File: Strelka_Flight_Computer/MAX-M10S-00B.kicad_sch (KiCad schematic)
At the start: 17 parts, among them IC2 MAX-M10S-00B

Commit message: Started design for V2
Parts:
- removed AE2: Antenna_Shield, Connector_Coaxial:U.FL_Hirose_U.FL-R-SMT-1_Vertical, symbol Device:Antenna_Shield
- removed JP2: UART_Switch, Footprints:UART_Switch, symbol UART_Switch:UART_Switch
- added AE1: Antenna_Shield, Footprints:STA-10201, symbol Device:Antenna_Shield
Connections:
- net GND: now also AE1.2 (Shield)
- net RF_IN: now also AE1.1 (A)
- net UBLOX_UART_RX: now also IC2.3 (RXD)
- net UBLOX_UART_TX: now also IC2.2 (TXD)
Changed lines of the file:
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@@
-    (stroke (width 0) (type default))
-  )
-  (wire (pts (xy 190.5 99.06) (xy 190.5 98.425))
-    (stroke (width 0) (type default))
-  )
-  (wire (pts (xy 190.5 102.235) (xy 194.31 102.235))
     (stroke (width 0) (type default))
   )
@@
     (stroke (width 0) (type default))
   )
-  (wire (pts (xy 190.5 98.425) (xy 194.31 98.425))
-    (stroke (width 0) (type default))
-  )
   (wire (pts (xy 53.975 102.235) (xy 53.975 104.14))
     (stroke (width 0) (type default))
@@
     (stroke (width 0) (type default))
   )
-  (wire (pts (xy 174.625 101.6) (xy 190.5 101.6))
+  (wire (pts (xy 174.625 101.6) (xy 192.405 101.6))
     (stroke (width 0) (type default))
   )
@@
     (stroke (width 0) (type default))
   )
-  (wire (pts (xy 209.55 102.235) (xy 211.455 102.235))
-    (stroke (width 0) (type default))
-  )
   (wire (pts (xy 67.945 162.56) (xy 67.945 163.195))
     (stroke (width 0) (type default))
@@
     (stroke (width 0) (type default))
   )
-  (wire (pts (xy 209.55 98.425) (xy 211.455 98.425))
-    (stroke (width 0) (type default))
-  )
   (wire (pts (xy 57.785 160.02) (xy 57.785 163.195))
     (stroke (width 0) (type default))
@@
     (stroke (width 0) (type default))
   )
-  (wire (pts (xy 174.625 99.06) (xy 190.5 99.06))
+  (wire (pts (xy 174.625 99.06) (xy 192.405 99.06))
     (stroke (width 0) (type default))
   )
@@
   )
   (wire (pts (xy 48.895 154.305) (xy 48.895 153.67))
-    (stroke (width 0) (type default))
-  )
-  (wire (pts (xy 190.5 101.6) (xy 190.5 102.235))
     (stroke (width 0) (type default))
   )
@@
     (effects (font (size 1.27 1.27)) (justify left))
   )
-  (hierarchical_label "UBLOX_UART_RX" (shape input) (at 211.455 98.425 0) (fields_autoplaced)
+  (hierarchical_label "UBLOX_UART_RX" (shape input) (at 192.405 99.06 0) (fields_autoplaced)
     (effects (font (size 1.27 1.27)) (justify left))
   )
@@
     (effects (font (size 1.27 1.27)) (justify left))
   )
-  (hierarchical_label "UBLOX_UART_TX" (shape input) (at 211.455 102.235 0) (fields_autoplaced)
+  (hierarchical_label "UBLOX_UART_TX" (shape input) (at 192.405 101.6 0) (fields_autoplaced)
     (effects (font (size 1.27 1.27)) (justify left))
   )
@@
     )
   )
-  (symbol (lib_id "UART_Switch:UART_Switch") (at 201.93 100.965 0) (unit 1)
-    (in_bom yes) (on_board yes) (dnp no)
-    (property "Reference" "JP2" (at 201.93 92.71 0)
-      (effects (font (size 1.27 1.27)))
-    )
-    (property "Value" "UART_Switch" (at 201.93 95.25 0)
-      (effects (font (size 1.27 1.27)))
-    )
-    (property "Footprint" "Footprints:UART_Switch" (at 201.93 100.965 0)
-      (effects (font (size 1.27 1.27)) hide)
-    )
-    (property "Datasheet" "" (at 201.93 100.965 0)
-      (effects (font (size 1.27 1.27)) hide)
-    )
-    (pin "1")
-    (pin "2")
-    (pin "3")
-    (pin "4")
-    (instances
-      (project "Strelka_Flight_Computer"
-        (path "/e63e39d7-6ac0-4ffd-8aa3-1841a4541b55/78f71895-bddb-4f64-a608-99074f2d1c44/139c9d95-fce8-4012-aeed-de926a08d12b"
-          (reference "JP2") (unit 1)
+  (symbol (lib_id "Device:Antenna_Shield") (at 35.56 71.12 0) (unit 1)
+    (in_bom yes) (on_board yes) (dnp no) (fields_autoplaced)
+    (property "Reference" "AE1" (at 39.1161 70.3385 0)
+      (effects (font (size 1.27 1.27)) (justify left))
+    )
+    (property "Value" "Antenna_Shield" (at 39.1161 73.1136 0)
+      (effects (font (size 1.27 1.27)) (justify left))
+    )
+    (property "Footprint" "Footprints:STA-10201" (at 35.56 68.58 0)
+      (effects (font (size 1.27 1.27)) hide)
+    )
+    (property "Datasheet" "https://datasheet.lcsc.com/lcsc/2111030930_STA-STA-10201_C2913580.pdf" (at 35.56 68.58 0)
+      (effects (font (size 1.27 1.27)) hide)
+    )
+    (property "LCSC#" "C2913580" (at 35.56 71.12 0)
+      (effects (font (size 1.27 1.27)) hide)
+    )
+    (pin "1")
+    (pin "2")
+    (instances
+      (project "Strelka_Flight_Computer"
+        (path "/e63e39d7-6ac0-4ffd-8aa3-1841a4541b55/72745e37-6398-4523-a0b8-fcae44c9df22"
+          (reference "AE1") (unit 1)
+        )
+        (path "/e63e39d7-6ac0-4ffd-8aa3-1841a4541b55/78f71895-bddb-4f64-a608-99074f2d1c44/139c9d95-fce8-4012-aeed-de926a08d12b"
+          (reference "AE2") (unit 1)
         )
       )
@@
         )
       )
-    )
-  )
-  (symbol (lib_id "Device:Antenna_Shield") (at 35.56 71.12 0) (unit 1)
-    (in_bom yes) (on_board yes) (dnp no) (fields_autoplaced)
-    (property "Reference" "AE2" (at 38.735 69.6503 0)
-      (effects (font (size 1.27 1.27)) (justify left))
-    )
-    (property "Value" "Antenna_Shield" (at 38.735 72.1872 0)
-      (effects (font (size 1.27 1.27)) (justify left))
-    )
-    (property "Footprint" "Connector_Coaxial:U.FL_Hirose_U.FL-R-SMT-1_Vertical" (at 35.56 68.58 0)
-      (effects (font (size 1.27 1.27)) hide)
-    )
-    (property "Datasheet" "~" (at 35.56 68.58 0)
-      (effects (font (size 1.27 1.27)) hide)
-    )
-    (property "LCSC#" "C88373" (at 35.56 71.12 0)
-      (effects (font (size 1.27 1.27)) hide)
-    )
-    (pin "1")
-    (pin "2")
-    (instances
-      (project "Strelka_Flight_Computer"
-        (path "/e63e39d7-6ac0-4ffd-8aa3-1841a4541b55/78f71895-bddb-4f64-a608-99074f2d1c44/139c9d95-fce8-4012-aeed-de926a08d12b"
-          (reference "AE2") (unit 1)
-        )
-      )

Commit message: Changed design rules
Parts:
- C36, C38, C39, C40: footprint Capacitor_SMD:C_0603_1608Metric -> Capacitor_SMD:C_0402_1005Metric
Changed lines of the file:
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@@
       (effects (font (size 1.27 1.27)) (justify left))
     )
-    (property "Footprint" "Capacitor_SMD:C_0603_1608Metric" (at 218.44 88.9 0)
+    (property "Footprint" "Capacitor_SMD:C_0402_1005Metric" (at 218.44 88.9 0)
       (effects (font (size 1.27 1.27)) hide)
     )
@@
       (effects (font (size 1.27 1.27)) (justify left))
     )
-    (property "Footprint" "Capacitor_SMD:C_0603_1608Metric" (at 207.01 88.9 0)
+    (property "Footprint" "Capacitor_SMD:C_0402_1005Metric" (at 207.01 88.9 0)
       (effects (font (size 1.27 1.27)) hide)
     )
@@
       (effects (font (size 1.27 1.27)) (justify left))
     )
-    (property "Footprint" "Capacitor_SMD:C_0603_1608Metric" (at 57.785 157.48 0)
+    (property "Footprint" "Capacitor_SMD:C_0402_1005Metric" (at 57.785 157.48 0)
       (effects (font (size 1.27 1.27)) hide)
     )
@@
       (effects (font (size 1.27 1.27)) (justify left))
     )
-    (property "Footprint" "Capacitor_SMD:C_0603_1608Metric" (at 48.895 156.845 0)
-      (effects (font (size 1.27 1.27)) hide)
-    )
+    (property "Footprint" "Capacitor_SMD:C_0402_1005Metric" (at 48.895 156.845 0)
+      (effects (font (size 1.27 1.27)) hide)
+    )

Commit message: Routing starting
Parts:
- removed R58: 0R, Resistor_SMD:R_0603_1608Metric, symbol Device:R_Small
- R56, R57: footprint Resistor_SMD:R_0603_1608Metric -> Resistor_SMD:R_0402_1005Metric
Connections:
- net PPS is gone; now on net TIMEPULSE: IC2.4 (TIMEPULSE), R57.1
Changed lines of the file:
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@@
     (stroke (width 0) (type default))
   )
-  (wire (pts (xy 214.63 111.76) (xy 217.17 111.76))
+  (wire (pts (xy 214.63 111.76) (xy 222.25 111.76))
     (stroke (width 0) (type default))
   )
@@
         (path "/e63e39d7-6ac0-4ffd-8aa3-1841a4541b55/78f71895-bddb-4f64-a608-99074f2d1c44/139c9d95-fce8-4012-aeed-de926a08d12b"
           (reference "BT2") (unit 1)
-        )
-      )
-    )
-  )
-  (symbol (lib_id "Device:R_Small") (at 219.71 111.76 90) (unit 1)
-    (in_bom yes) (on_board yes) (dnp no)
-    (property "Reference" "R58" (at 218.5416 110.2614 0)
-      (effects (font (size 1.27 1.27)) (justify left))
-    )
-    (property "Value" "0R" (at 220.853 110.2614 0)
-      (effects (font (size 1.27 1.27)) (justify left))
-    )
-    (property "Footprint" "Resistor_SMD:R_0603_1608Metric" (at 219.71 111.76 0)
-      (effects (font (size 1.27 1.27)) hide)
-    )
-    (property "Datasheet" "~" (at 219.71 111.76 0)
-      (effects (font (size 1.27 1.27)) hide)
-    )
-    (pin "1")
-    (pin "2")
-    (instances
-      (project "Strelka_Flight_Computer"
-        (path "/e63e39d7-6ac0-4ffd-8aa3-1841a4541b55/78f71895-bddb-4f64-a608-99074f2d1c44/139c9d95-fce8-4012-aeed-de926a08d12b"
-          (reference "R58") (unit 1)
         )
       )
@@
       (effects (font (size 1.27 1.27)) (justify left))
     )
-    (property "Footprint" "Resistor_SMD:R_0603_1608Metric" (at 67.945 149.86 0)
+    (property "Footprint" "Resistor_SMD:R_0402_1005Metric" (at 67.945 149.86 0)
       (effects (font (size 1.27 1.27)) hide)
     )
@@
       (effects (font (size 1.27 1.27)) (justify left))
     )
-    (property "Footprint" "Resistor_SMD:R_0603_1608Metric" (at 214.63 114.935 0)
-      (effects (font (size 1.27 1.27)) hide)
-    )
+    (property "Footprint" "Resistor_SMD:R_0402_1005Metric" (at 214.63 114.935 0)
+      (effects (font (size 1.27 1.27)) hide)
+    )

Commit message: Continued routing
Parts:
- C37: now not fitted
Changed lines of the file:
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@@
   )
   (symbol (lib_id "Device:C_Small") (at 53.975 107.315 0) (unit 1)
-    (in_bom yes) (on_board yes) (dnp no)
+    (in_bom yes) (on_board yes) (dnp yes)
     (property "Reference" "C37" (at 56.515 104.775 0)
       (effects (font (size 1.27 1.27)) (justify left))

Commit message: Routing complete
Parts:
- removed C36: 100n, Capacitor_SMD:C_0402_1005Metric, symbol Device:C_Small
- D12: value LED_BLUE -> LED_GREEN; LCSC (none) -> C72043
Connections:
- net +3V3 renamed +3.3V
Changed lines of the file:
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@@
 (kicad_sch (version 20230121) (generator eeschema)
   (paper "A4")
+  (junction (at 212.725 83.82) (diameter 0) (color 0 0 0 0)
+  )
   (junction (at 177.165 86.36) (diameter 0) (color 0 0 0 0)
   )
@@
   (junction (at 213.36 91.44) (diameter 0) (color 0 0 0 0)
   )
-  (junction (at 213.36 83.82) (diameter 0) (color 0 0 0 0)
-  )
   (junction (at 57.785 153.67) (diameter 0) (color 0 0 0 0)
   )
   (junction (at 62.865 163.195) (diameter 0) (color 0 0 0 0)
-  )
-  (junction (at 57.785 163.195) (diameter 0) (color 0 0 0 0)
   )
   (junction (at 53.975 104.14) (diameter 0) (color 0 0 0 0)
@@
     (stroke (width 0) (type default))
   )
-  (wire (pts (xy 48.895 159.385) (xy 48.895 163.195))
-    (stroke (width 0) (type default))
-  )
   (wire (pts (xy 53.975 102.235) (xy 53.975 104.14))
     (stroke (width 0) (type default))
   )
-  (wire (pts (xy 48.895 163.195) (xy 57.785 163.195))
-    (stroke (width 0) (type default))
-  )
   (wire (pts (xy 53.975 104.14) (xy 60.96 104.14))
     (stroke (width 0) (type default))
@@
     (stroke (width 0) (type default))
   )
+  (wire (pts (xy 212.725 83.82) (xy 218.44 83.82))
+    (stroke (width 0) (type default))
+  )
   (wire (pts (xy 53.975 90.17) (xy 53.975 84.455))
     (stroke (width 0) (type default))
@@
     (stroke (width 0) (type default))
   )
-  (wire (pts (xy 48.895 153.67) (xy 57.785 153.67))
-    (stroke (width 0) (type default))
-  )
   (wire (pts (xy 57.785 160.02) (xy 57.785 163.195))
     (stroke (width 0) (type default))
@@
     (stroke (width 0) (type default))
   )
-  (wire (pts (xy 213.36 83.82) (xy 218.44 83.82))
+  (wire (pts (xy 207.01 83.82) (xy 212.725 83.82))
     (stroke (width 0) (type default))
   )
@@
     (stroke (width 0) (type default))
   )
-  (wire (pts (xy 48.895 154.305) (xy 48.895 153.67))
-    (stroke (width 0) (type default))
-  )
   (wire (pts (xy 57.785 153.67) (xy 67.945 153.67))
     (stroke (width 0) (type default))
@@
   )
   (wire (pts (xy 57.785 153.67) (xy 57.785 154.94))
-    (stroke (width 0) (type default))
-  )
-  (wire (pts (xy 207.01 83.82) (xy 213.36 83.82))
     (stroke (width 0) (type default))
   )
@@
         (path "/e63e39d7-6ac0-4ffd-8aa3-1841a4541b55/78f71895-bddb-4f64-a608-99074f2d1c44/139c9d95-fce8-4012-aeed-de926a08d12b"
           (reference "BT2") (unit 1)
+        )
+      )
+    )
+  )
+  (symbol (lib_name "+3.3V_1") (lib_id "power:+3.3V") (at 200.025 86.36 0) (unit 1)
+    (in_bom yes) (on_board yes) (dnp no) (fields_autoplaced)
+    (property "Reference" "#PWR015" (at 200.025 90.17 0)
+      (effects (font (size 1.27 1.27)) hide)
+    )
+    (property "Value" "+3.3V" (at 200.025 82.931 0)
+      (effects (font (size 1.27 1.27)))
+    )
+    (property "Footprint" "" (at 200.025 86.36 0)
+      (effects (font (size 1.27 1.27)) hide)
+    )
+    (property "Datasheet" "" (at 200.025 86.36 0)
+      (effects (font (size 1.27 1.27)) hide)
+    )
+    (pin "1")
+    (instances
+      (project "Strelka_Flight_Computer"
+        (path "/e63e39d7-6ac0-4ffd-8aa3-1841a4541b55/0daddb18-1491-4767-9ffd-66c8a8ce3cbd"
+          (reference "#PWR015") (unit 1)
+        )
+        (path "/e63e39d7-6ac0-4ffd-8aa3-1841a4541b55/78f71895-bddb-4f64-a608-99074f2d1c44/139c9d95-fce8-4012-aeed-de926a08d12b"
+          (reference "#PWR016") (unit 1)
         )
       )
@@
     )
   )
-  (symbol (lib_id "power:+3.3V") (at 200.025 86.36 0) (unit 1)
-    (in_bom yes) (on_board yes) (dnp no) (fields_autoplaced)
-    (property "Reference" "#PWR0210" (at 200.025 90.17 0)
-      (effects (font (size 1.27 1.27)) hide)
-    )
-    (property "Value" "+3.3V" (at 200.025 82.7842 0)
-      (effects (font (size 1.27 1.27)))
-    )
-    (property "Footprint" "" (at 200.025 86.36 0)
-      (effects (font (size 1.27 1.27)) hide)
-    )
-    (property "Datasheet" "" (at 200.025 86.36 0)
-      (effects (font (size 1.27 1.27)) hide)
-    )
-    (pin "1")
-    (instances
-      (project "Strelka_Flight_Computer"
-        (path "/e63e39d7-6ac0-4ffd-8aa3-1841a4541b55/78f71895-bddb-4f64-a608-99074f2d1c44/139c9d95-fce8-4012-aeed-de926a08d12b"
-          (reference "#PWR0210") (unit 1)
-        )
-      )
-    )
-  )
   (symbol (lib_id "Device:C_Small") (at 57.785 157.48 0) (unit 1)
     (in_bom yes) (on_board yes) (dnp no)
@@
     )
   )
-  (symbol (lib_id "power:+3.3V") (at 213.36 83.82 0) (unit 1)
-    (in_bom yes) (on_board yes) (dnp no) (fields_autoplaced)
-    (property "Reference" "#PWR0209" (at 213.36 87.63 0)
-      (effects (font (size 1.27 1.27)) hide)
-    )
-    (property "Value" "+3.3V" (at 213.36 80.2442 0)
-      (effects (font (size 1.27 1.27)))
-    )
-    (property "Footprint" "" (at 213.36 83.82 0)
-      (effects (font (size 1.27 1.27)) hide)
-    )
-    (property "Datasheet" "" (at 213.36 83.82 0)
-      (effects (font (size 1.27 1.27)) hide)
-    )
-    (pin "1")
-    (instances
-      (project "Strelka_Flight_Computer"
-        (path "/e63e39d7-6ac0-4ffd-8aa3-1841a4541b55/78f71895-bddb-4f64-a608-99074f2d1c44/139c9d95-fce8-4012-aeed-de926a08d12b"
-          (reference "#PWR0209") (unit 1)
+  (symbol (lib_name "+3.3V_1") (lib_id "power:+3.3V") (at 212.725 83.82 0) (unit 1)
+    (in_bom yes) (on_board yes) (dnp no) (fields_autoplaced)
+    (property "Reference" "#PWR015" (at 212.725 87.63 0)
+      (effects (font (size 1.27 1.27)) hide)
+    )
+    (property "Value" "+3.3V" (at 212.725 80.391 0)
+      (effects (font (size 1.27 1.27)))
+    )
+    (property "Footprint" "" (at 212.725 83.82 0)
+      (effects (font (size 1.27 1.27)) hide)
+    )
+    (property "Datasheet" "" (at 212.725 83.82 0)
+      (effects (font (size 1.27 1.27)) hide)
+    )
+    (pin "1")
+    (instances
+      (project "Strelka_Flight_Computer"
+        (path "/e63e39d7-6ac0-4ffd-8aa3-1841a4541b55/0daddb18-1491-4767-9ffd-66c8a8ce3cbd"
+          (reference "#PWR015") (unit 1)
+        )
+        (path "/e63e39d7-6ac0-4ffd-8aa3-1841a4541b55/78f71895-bddb-4f64-a608-99074f2d1c44/139c9d95-fce8-4012-aeed-de926a08d12b"
+          (reference "#PWR017") (unit 1)
         )
       )
@@
         (path "/e63e39d7-6ac0-4ffd-8aa3-1841a4541b55/78f71895-bddb-4f64-a608-99074f2d1c44/139c9d95-fce8-4012-aeed-de926a08d12b"
           (reference "#PWR0206") (unit 1)
-        )
-      )
-    )
-  )
-  (symbol (lib_id "power:+3.3V") (at 60.325 140.97 0) (unit 1)
-    (in_bom yes) (on_board yes) (dnp no) (fields_autoplaced)
-    (property "Reference" "#PWR0214" (at 60.325 144.78 0)
-      (effects (font (size 1.27 1.27)) hide)
-    )
-    (property "Value" "+3.3V" (at 60.325 137.3942 0)
-      (effects (font (size 1.27 1.27)))
-    )
-    (property "Footprint" "" (at 60.325 140.97 0)
-      (effects (font (size 1.27 1.27)) hide)
-    )
-    (property "Datasheet" "" (at 60.325 140.97 0)
-      (effects (font (size 1.27 1.27)) hide)
-    )
-    (pin "1")
-    (instances
-      (project "Strelka_Flight_Computer"
-        (path "/e63e39d7-6ac0-4ffd-8aa3-1841a4541b55/78f71895-bddb-4f64-a608-99074f2d1c44/139c9d95-fce8-4012-aeed-de926a08d12b"
-          (reference "#PWR0214") (unit 1)
         )
       )
@@
     )
   )
-  (symbol (lib_id "Device:C_Small") (at 48.895 156.845 0) (unit 1)
-    (in_bom yes) (on_board yes) (dnp no)
-    (property "Reference" "C36" (at 51.435 154.305 0)
-      (effects (font (size 1.27 1.27)) (justify left))
-    )
-    (property "Value" "100n" (at 51.435 156.845 0)
-      (effects (font (size 1.27 1.27)) (justify left))
-    )
-    (property "Footprint" "Capacitor_SMD:C_0402_1005Metric" (at 48.895 156.845 0)
-      (effects (font (size 1.27 1.27)) hide)
-    )
-    (property "Datasheet" "~" (at 48.895 156.845 0)
-      (effects (font (size 1.27 1.27)) hide)
-    )
-    (pin "1")
-    (pin "2")
-    (instances
-      (project "Strelka_Flight_Computer"
-        (path "/e63e39d7-6ac0-4ffd-8aa3-1841a4541b55/78f71895-bddb-4f64-a608-99074f2d1c44/139c9d95-fce8-4012-aeed-de926a08d12b"
-          (reference "C36") (unit 1)
-        )
-      )
-    )
-  )
   (symbol (lib_id "Device:LED_Small") (at 214.63 120.65 90) (unit 1)
     (in_bom yes) (on_board yes) (dnp no)
@@
       (effects (font (size 1.27 1.27)) (justify right))
     )
-    (property "Value" "LED_BLUE" (at 216.408 121.793 90)
+    (property "Value" "LED_GREEN" (at 216.408 121.793 90)
       (effects (font (size 1.27 1.27)) (justify right))
     )
@@
       (effects (font (size 1.27 1.27)) hide)
     )
+    (property "LCSC" "C72043" (at 214.63 120.65 90)
+      (effects (font (size 1.27 1.27)) hide)
+    )
     (pin "1")
     (pin "2")
@@
         )
       )
+    )
+  )
+  (symbol (lib_name "+3.3V_1") (lib_id "power:+3.3V") (at 60.325 140.97 0) (unit 1)
+    (in_bom yes) (on_board yes) (dnp no) (fields_autoplaced)
+    (property "Reference" "#PWR015" (at 60.325 144.78 0)
+      (effects (font (size 1.27 1.27)) hide)
+    )
+    (property "Value" "+3.3V" (at 60.325 137.541 0)
+      (effects (font (size 1.27 1.27)))
+    )
+    (property "Footprint" "" (at 60.325 140.97 0)
+      (effects (font (size 1.27 1.27)) hide)
+    )
+    (property "Datasheet" "" (at 60.325 140.97 0)
+      (effects (font (size 1.27 1.27)) hide)
+    )
+    (pin "1")
+    (instances
+      (project "Strelka_Flight_Computer"
+        (path "/e63e39d7-6ac0-4ffd-8aa3-1841a4541b55/0daddb18-1491-4767-9ffd-66c8a8ce3cbd"
+          (reference "#PWR015") (unit 1)
+        )
+        (path "/e63e39d7-6ac0-4ffd-8aa3-1841a4541b55/78f71895-bddb-4f64-a608-99074f2d1c44/139c9d95-fce8-4012-aeed-de926a08d12b"
+          (reference "#PWR018") (unit 1)
+        )
+      )

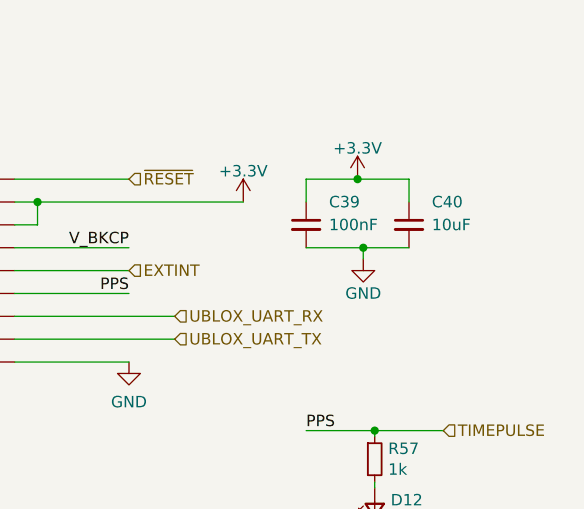
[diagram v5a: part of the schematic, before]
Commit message: Created BOM
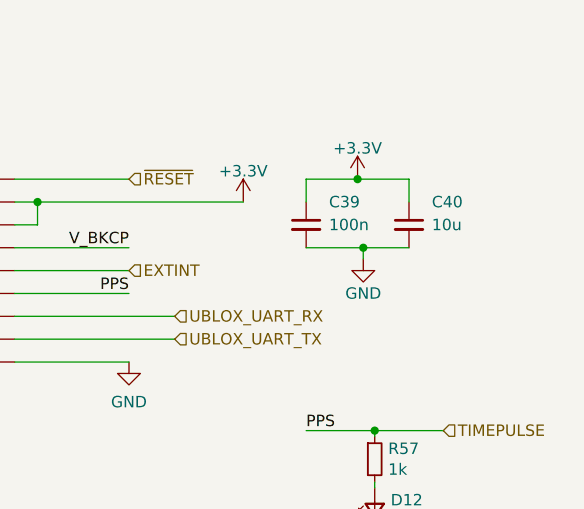
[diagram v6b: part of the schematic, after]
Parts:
- AE1: LCSC (none) -> C2913580; LCSC# C2913580 -> (none)
- C39: value 100nF -> 100n
- C40: value 10uF -> 10u
- D10: LCSC (none) -> C558621; LCSC# C558621 -> (none)
- D11: LCSC (none) -> C37704; LCSC# C37704 -> (none)
- FB3: LCSC (none) -> C279553; LCSC# C279553 -> (none)
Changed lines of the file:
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@@
       (effects (font (size 1.27 1.27)) (justify left))
     )
-    (property "Value" "10uF" (at 220.98 88.9 0)
+    (property "Value" "10u" (at 220.98 88.9 0)
       (effects (font (size 1.27 1.27)) (justify left))
     )
@@
       (effects (font (size 1.27 1.27)) (justify left))
     )
-    (property "Value" "100nF" (at 209.55 88.9 0)
+    (property "Value" "100n" (at 209.55 88.9 0)
       (effects (font (size 1.27 1.27)) (justify left))
     )
@@
       (effects (font (size 1.27 1.27)) hide)
     )
-    (property "LCSC#" "C279553" (at 53.975 92.71 0)
+    (property "LCSC" "C279553" (at 53.975 92.71 0)
       (effects (font (size 1.27 1.27)) hide)
     )
@@
       (effects (font (size 1.27 1.27)) hide)
     )
-    (property "LCSC#" "C558621" (at 35.56 92.71 90)
+    (property "LCSC" "C558621" (at 35.56 92.71 90)
       (effects (font (size 1.27 1.27)) hide)
     )
@@
       (effects (font (size 1.27 1.27)) hide)
     )
-    (property "LCSC#" "C2913580" (at 35.56 71.12 0)
+    (property "LCSC" "C2913580" (at 35.56 71.12 0)
       (effects (font (size 1.27 1.27)) hide)
     )
@@
       (effects (font (size 1.27 1.27)) hide)
     )
-    (property "LCSC#" "C37704" (at 67.945 140.97 0)
-      (effects (font (size 1.27 1.27)) hide)
-    )
+    (property "LCSC" "C37704" (at 67.945 140.97 0)
+      (effects (font (size 1.27 1.27)) hide)
+    )

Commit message: Added LCSC mpn to all relevent parts
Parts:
- C38: LCSC (none) -> 2.2u
- C39: LCSC (none) -> C1525
- C40: LCSC (none) -> C15525
- R55: LCSC (none) -> C17168
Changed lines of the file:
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@@
+      (effects (font (size 1.27 1.27)) hide)
+    )
+    (property "LCSC" "C15525" (at 218.44 88.9 0)
       (effects (font (size 1.27 1.27)) hide)
     )
@@
     )
     (property "Datasheet" "~" (at 207.01 88.9 0)
+      (effects (font (size 1.27 1.27)) hide)
+    )
+    (property "LCSC" " C1525" (at 207.01 88.9 0)
       (effects (font (size 1.27 1.27)) hide)
     )
@@
       (effects (font (size 1.27 1.27)) hide)
     )
+    (property "LCSC" "2.2u" (at 57.785 157.48 0)
+      (effects (font (size 1.27 1.27)) hide)
+    )
     (pin "1")
     (pin "2")
@@
       (effects (font (size 1.27 1.27)) hide)
     )
+    (property "LCSC" " C17168" (at 53.975 99.695 0)
+      (effects (font (size 1.27 1.27)) hide)
+    )
